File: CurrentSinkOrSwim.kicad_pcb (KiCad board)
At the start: 2 copper layers, 41.7 x 47.8 mm, 23 parts, among them P1 CONN_01X01, P101 CONN_01X02, P102 CONN_01X03, P103 CONN_01X02, Q401 BUK9575, U201 LMV358, U301 LM2931D-R

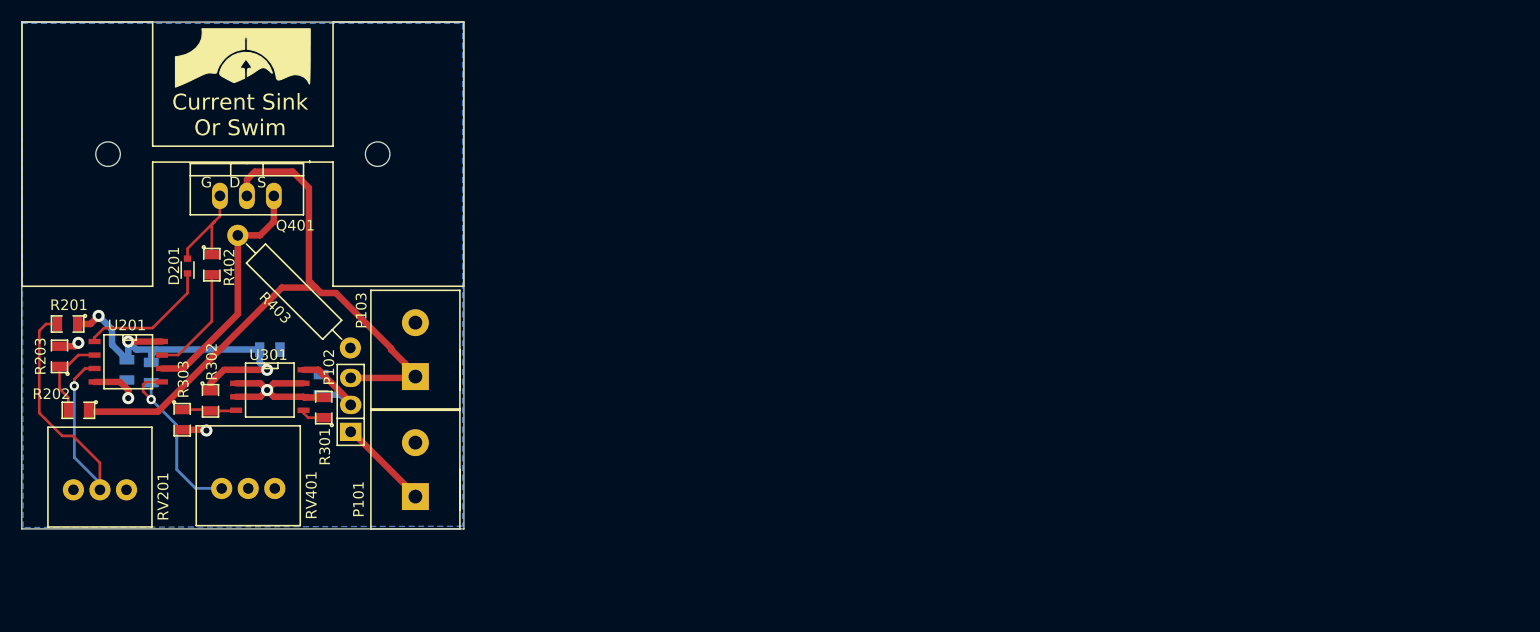
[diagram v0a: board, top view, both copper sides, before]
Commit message: Removed previous layout so now you can try it at home
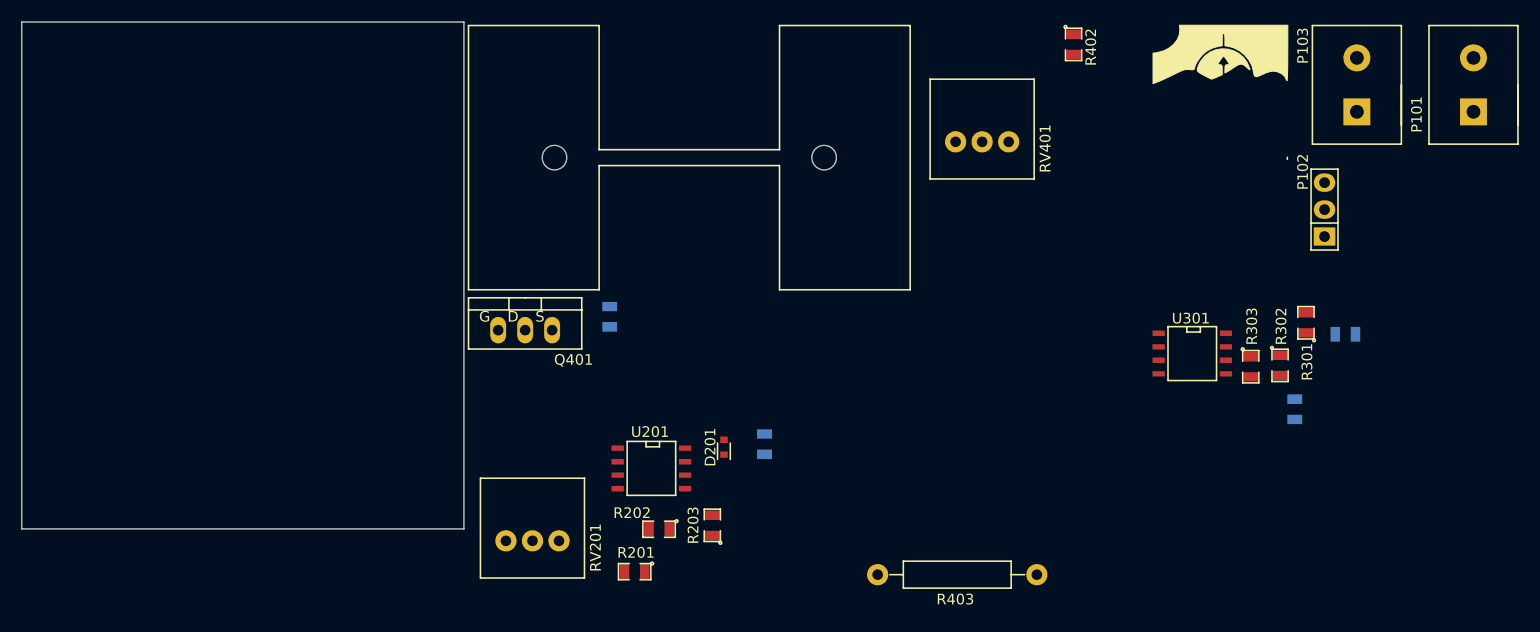
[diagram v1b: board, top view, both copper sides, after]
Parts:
- moved P101 106.1 mm to (242.9, 41.7)
- moved C302 101.3 mm to (230.9, 65.2)
- moved R302 100.8 mm to (224.7, 68.2)
- moved R303 100.8 mm to (221.9, 68.3)
- moved P102 93.6 mm to (228.9, 53.5)
- moved R301 92.9 mm to (227.1, 64.1)
- moved P103 92.1 mm to (231.9, 41.7)
- moved G*** 92.1 mm to (219.1, 42.5)
- moved C301 91.8 mm to (226.1, 72.3)
- moved U301 87.0 mm to (216.4, 67.0)
- moved R402 83.8 mm to (205.3, 37.9)
- moved RV401 76.5 mm to (196.6, 47.1)
- moved R403 67.9 mm to (194.3, 87.9), turned to 0 degrees
- moved R203 63.5 mm to (171.2, 83.2)
- moved C201 60.5 mm to (176.1, 75.6)
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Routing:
- net /Current Control/Current_Sink+: track 63.5 -> 0.00 mm
- net 2.7V: track 35.3 -> 0.00 mm, vias 3 -> 0
- net Net-(R201-Pad2): track 33.7 -> 0.00 mm, vias 1 -> 0
- net GND: track 24.5 -> 0.00 mm, vias 4 -> 0
- net Net-(Q401-PadS): track 23.0 -> 0.00 mm
- net Net-(R401-Pad2): track 17.9 -> 0.00 mm, vias 1 -> 0
- net Net-(D201-Pad2): track 12.7 -> 0.00 mm
- net Net-(R402-Pad2): track 10.4 -> 0.00 mm
- net /Current Control/FET_Gate: track 10.4 -> 0.00 mm
- net /Power Regulation/Vin: track 10.0 -> 0.00 mm
- net Net-(P101-Pad1): track 8.70 -> 0.00 mm
- net Net-(R202-Pad2): track 8.31 -> 0.00 mm
- net Net-(R302-Pad2): track 5.16 -> 0.00 mm
- net Net-(R301-Pad1): track 2.34 -> 0.00 mm
- removed copper zone on B.Cu, net GND
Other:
- board text removed: "Current Sink Or Swim"
